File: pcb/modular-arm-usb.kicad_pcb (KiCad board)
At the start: 2 copper layers, 50 x 22 mm, 30 parts, among them CON1 SWD, IC1 LPC11U14FBD48, P1 USB, P2 LED, P3 BATT, P4 GPIO, P5 gnd, P6 GPIO2, SW1 SW_SPDT, SW2 SW_PUSH_ALT, U2 MCP1700T, U3 nRF24L01+, X1 16M xtal

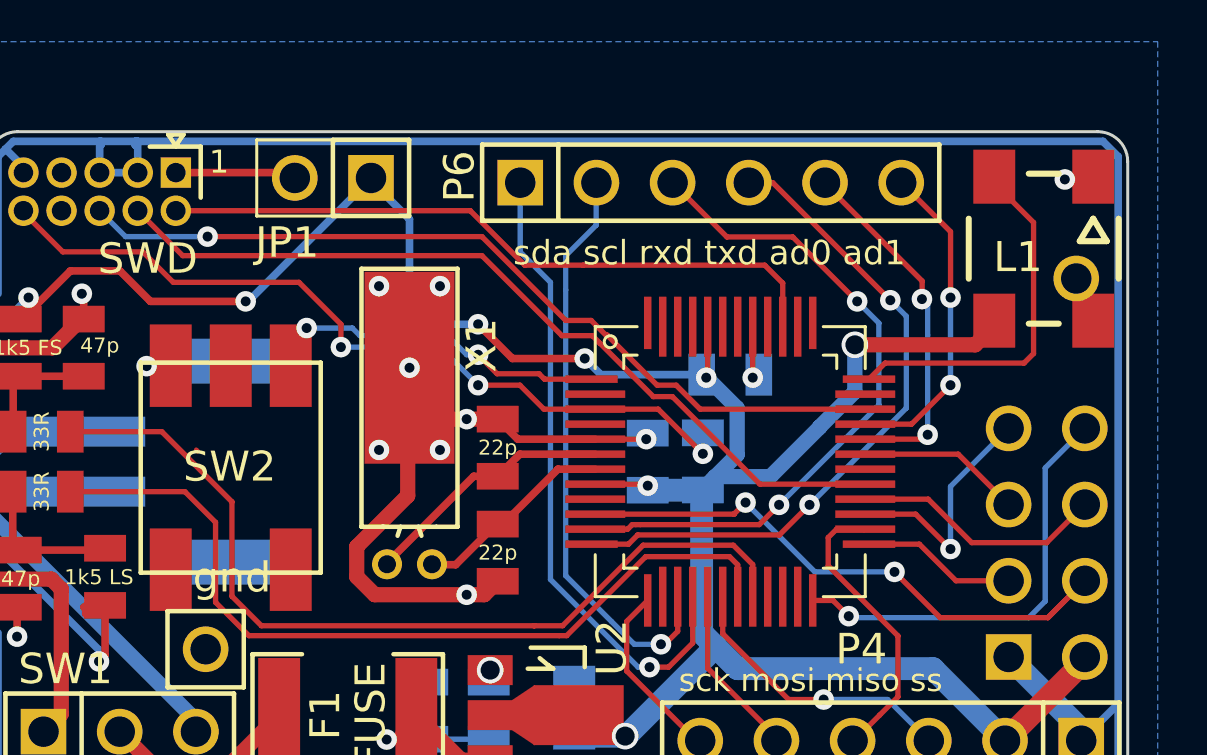
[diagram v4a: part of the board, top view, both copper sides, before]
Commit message: moved TXD and RXD to pins that give shorter traces, and attempted to route USB_CONNECT / implement SoftConnect, but gave up
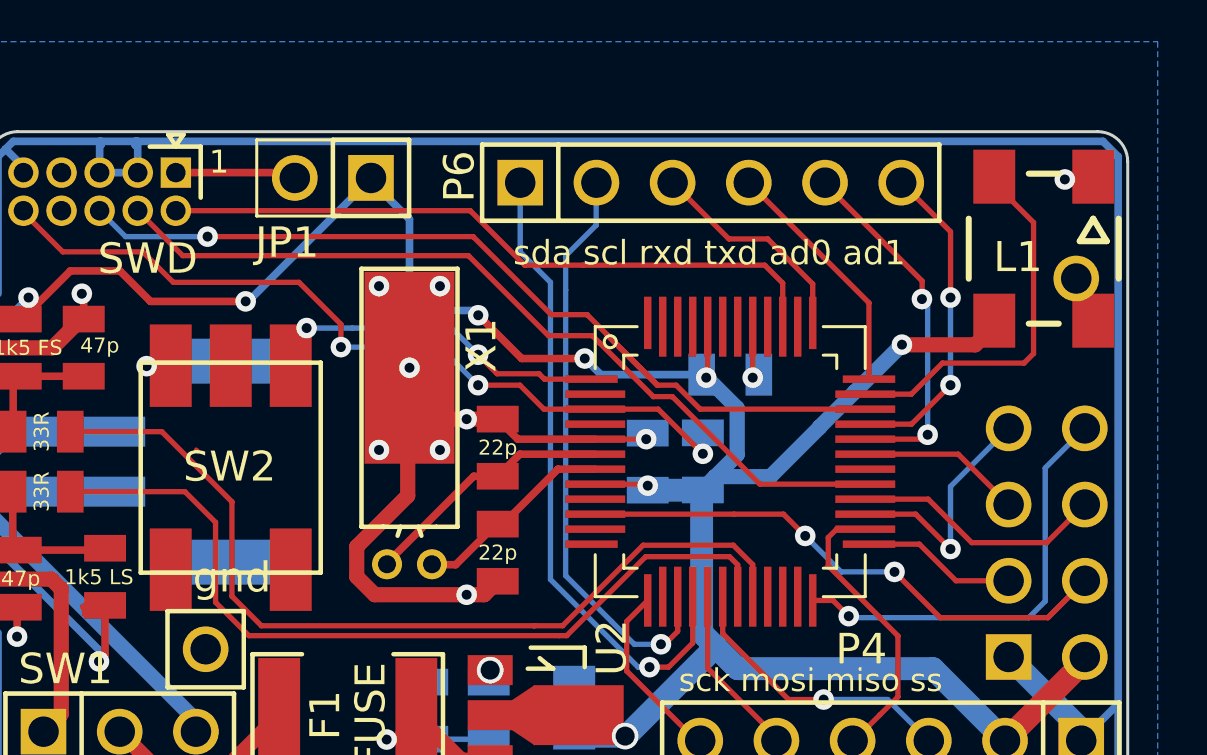
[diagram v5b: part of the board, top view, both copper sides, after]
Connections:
- IC1 pad 11: /lpc-mcu/RXD -> Net-(IC1-Pad11)
- IC1 pad 12: /lpc-mcu/TXD -> Net-(IC1-Pad12)
- IC1 pad 35: /lpc-mcu/AD3 -> /lpc-mcu/LED_INPUT
- IC1 pad 36: /lpc-mcu/LED_INPUT -> /lpc-mcu/TXD
- IC1 pad 37: Net-(IC1-Pad37) -> /lpc-mcu/RXD
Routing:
- net /lpc-mcu/RXD: track 23.6 -> 7.39 mm, vias 2 -> 0
- net /lpc-mcu/TXD: track 22.5 -> 8.21 mm, vias 2 -> 0
- net /lpc-mcu/SWO: track 28.5 -> 30.8 mm
- net Net-(IC1-Pad11): track 0.00 -> 0.90 mm
- net 3V3: track 104.0 -> 103.1 mm

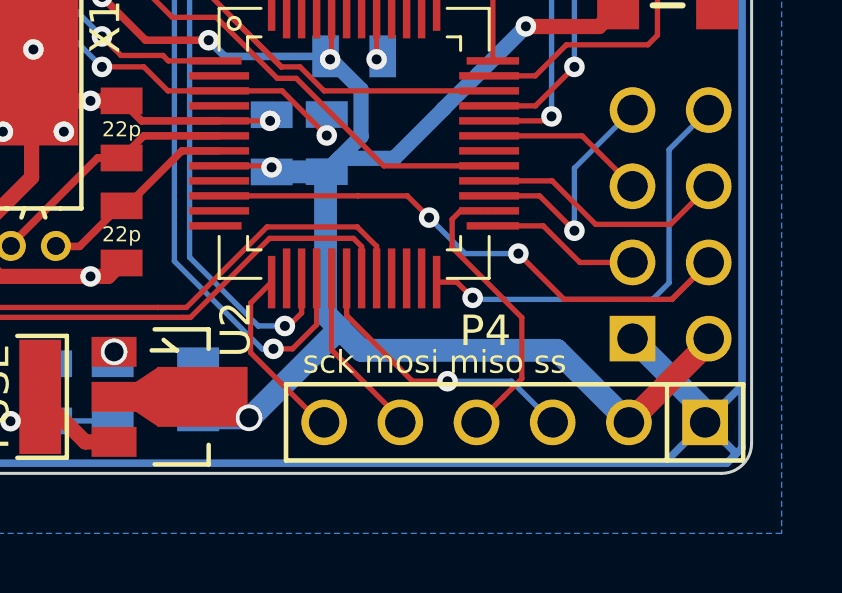
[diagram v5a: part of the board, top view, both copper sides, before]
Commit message: added a big empty track segment in case we want access to USB_CONNECT in an emergency
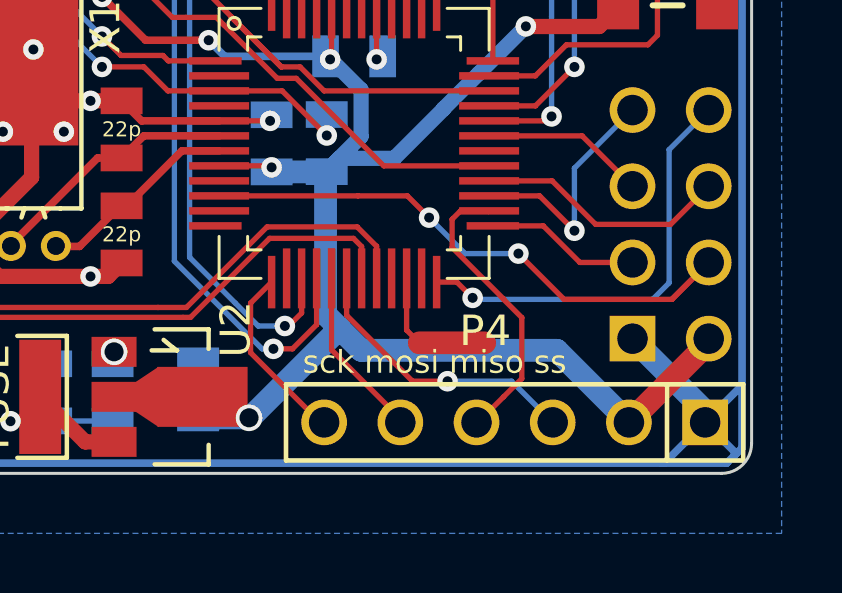
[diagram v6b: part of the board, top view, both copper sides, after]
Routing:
- net LPC_nUSB_CONNECT: track 0.00 -> 4.50 mm

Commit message: gerbers for oshpark order
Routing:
- net 3V3: track 103.1 -> 104.9 mm
